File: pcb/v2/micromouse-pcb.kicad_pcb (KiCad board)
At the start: 2 copper layers, 120 x 80 mm, 46 parts, among them J1_MotorEncoder1 Conn_01x06, J2_MotorEncoder1 Conn_01x06, J3 Conn_01x08, J4 Conn_01x08, Q1 BS170, Q2 TEFT4300, Q3 BS170, Q4 TEFT4300, Q5 BS170, Q6 TEFT4300, Q7 BS170, Q8 TEFT4300, SW1 SW_SPDT, U0 Teensy 4.1, U2 L7805

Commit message: should be version after design review
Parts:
- added D5: LED, LED_THT:LED_D5.0mm, F.Cu at (1.46, 80.4)
- added D6: LED, LED_THT:LED_D5.0mm, F.Cu at (1.46, 87.8)
- added R1_1: R_US, Resistor_SMD:R_1206_3216Metric_Pad1.30x1.75mm_HandSolder, F.Cu at (9.45, 78.3)
- added R1_2: R_US, Resistor_SMD:R_1206_3216Metric_Pad1.30x1.75mm_HandSolder, F.Cu at (9.45, 81.6)
- C1, C2, R1_750: moved to B.Cu
- moved C1 1.10 mm to (24.5, 83.1)
- moved C2 1.10 mm to (21.0, 83.1), turned to -90 degrees
- moved R1_750 0.10 mm to (28.5, 83.0)
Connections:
- SW1 pad 1: Net-(SW1-A) -> 7.4V
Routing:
- net Net-(SW1-A): track 12.0 -> 0.00 mm
- net 7.4V: track 30.2 -> 42.2 mm
- net GND: track 28.7 -> 22.3 mm, vias 6 -> 5

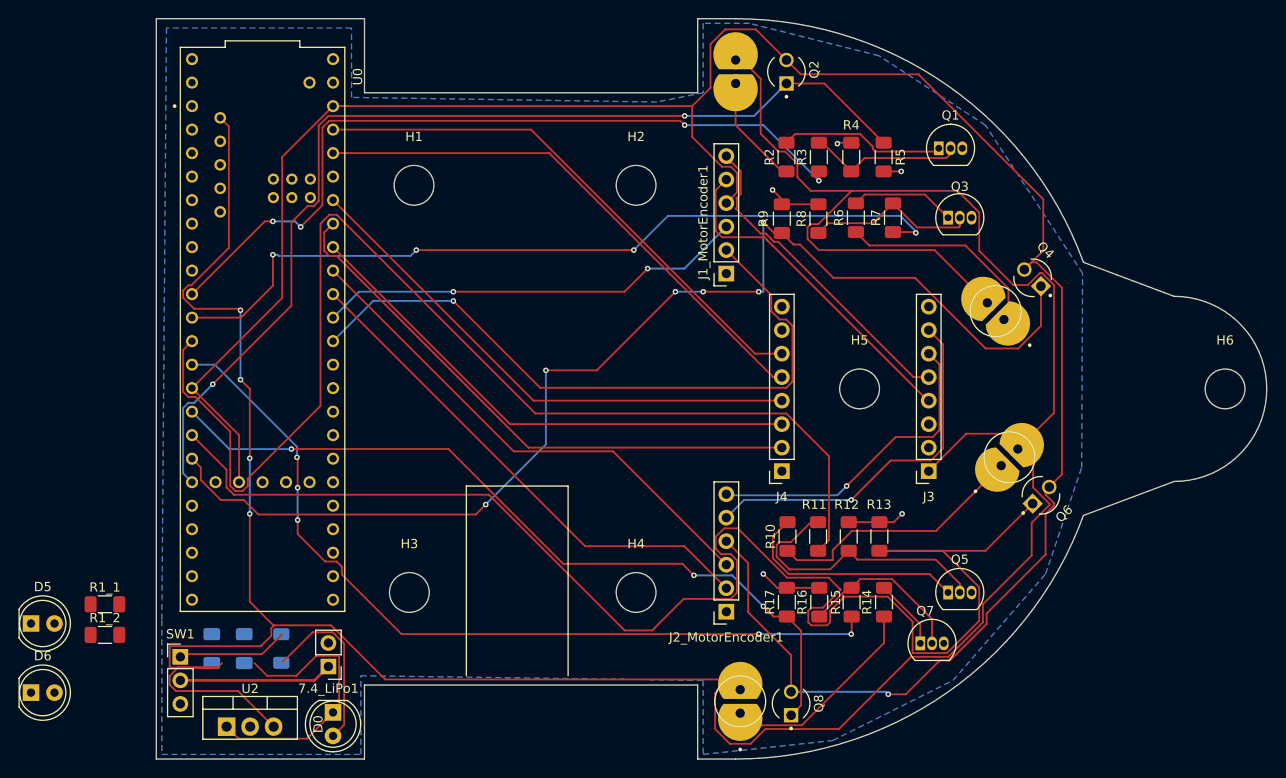
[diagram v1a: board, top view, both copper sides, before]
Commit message: fixed footprint and silkscreens
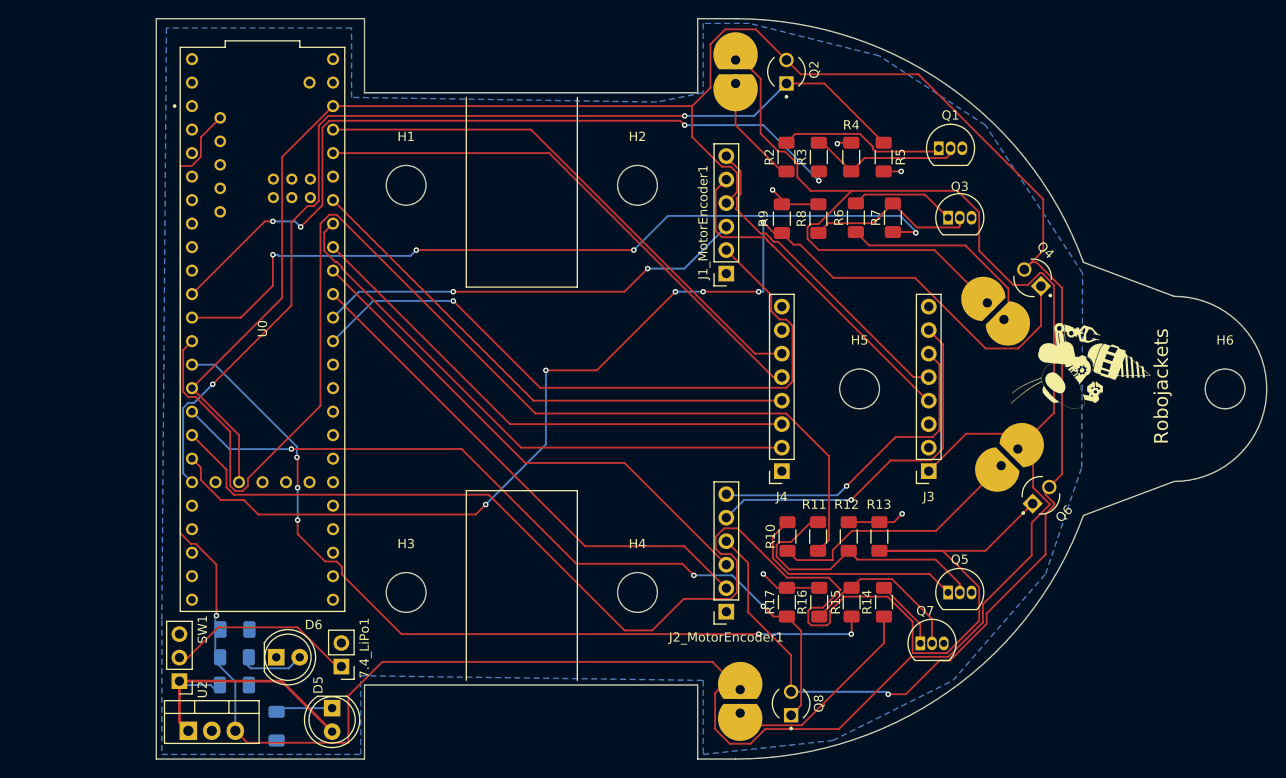
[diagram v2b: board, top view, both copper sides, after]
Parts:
- removed D0: LED, LED_THT:LED_D5.0mm
- removed R1_750: R_US, Resistor_SMD:R_1206_3216Metric_Pad1.30x1.75mm_HandSolder
- added ?: , symbols:ROBOBUZZ_0.8X, F.Cu at (122.5, 53.6)
- R1_1, R1_2: moved to B.Cu
- moved D5 33.8 mm to (34.0, 89.5), turned to -90 degrees
- moved D6 26.8 mm to (28.0, 84.0)
- moved R1_1 22.8 mm to (28.0, 91.5), turned to 90 degrees
- moved R1_2 14.2 mm to (23.4, 84.0)
- moved U2 4.16 mm to (18.5, 92.0)
- moved C1 4.08 mm to (23.4, 87.0), turned to 0 degrees
- moved C2 3.24 mm to (23.5, 81.0), turned to 0 degrees
- moved SW1 2.62 mm to (17.5, 86.6), turned to 180 degrees
- moved 7.4_LiPo1 1.40 mm to (35.0, 85.0)
- moved H1 0.85 mm to (42.0, 33.0)
- moved H3 0.35 mm to (42.0, 77.0)
- moved H2 0.15 mm to (67.0, 33.0)
- moved H4 0.15 mm to (67.0, 77.0)
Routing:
- net 5V: track 339.3 -> 316.5 mm, vias 4 -> 1
- net Net-(D0-A): track 19.0 -> 0.00 mm
- net 7.4V: track 42.2 -> 28.3 mm
- net Net-(D6-A): track 0.00 -> 6.79 mm
- net Net-(D5-K): track 0.00 -> 6.31 mm
- net Net-(7.4_LiPo1-+): track 16.6 -> 19.8 mm
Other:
- board text added: "Robojackets"
